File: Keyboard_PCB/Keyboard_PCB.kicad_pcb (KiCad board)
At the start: 6 copper layers, 65 x 103 mm, 119 parts, among them J2 Conn_ARM_SWD_TagConnect_TC2030, J3 CH_USB_C, SW1 BOOT, SW10 7, SW11 8, SW12 9, SW13 10, SW14 11, SW15 EC11E15244G1, SW2 NRST, SW3 0, SW4 1, SW5 2, SW6 3, SW7 4, SW8 5, SW9 6, U1 S40FC002C1B2I00000, U2 STM32U385VGI6, U3 CC2500, U4 2450BM15B0003001E, U5 USBLC6-2SC6, U6 ISL91127IRAZ, U7 MCP73833, Y1 26MHz, Y2 25MHz, Y3 32.786KHz

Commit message: Grid diode layout
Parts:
- added D10: D_Small, Marijn:SOD-523F, B.Cu at (208.0, 206.8)
- added D11: D_Small, Marijn:SOD-523F, B.Cu at (227.0, 206.8)
- added D12: D_Small, Marijn:SOD-523F, B.Cu at (188.9, 225.9)
- added D13: D_Small, Marijn:SOD-523F, B.Cu at (208.0, 225.9)
- added D14: D_Small, Marijn:SOD-523F, B.Cu at (227.0, 225.9)
- added D15: ~, Marijn:SOD-523F, F.Cu at (239.5, 154.6)
- added D3: D_Small, Marijn:SOD-523F, B.Cu at (196.5, 180.4)
- added D4: D_Small, Marijn:SOD-523F, B.Cu at (215.6, 180.4)
- added D5: D_Small, Marijn:SOD-523F, B.Cu at (234.6, 180.4)
- added D6: D_Small, Marijn:SOD-523F, B.Cu at (188.9, 187.8)
- added D7: D_Small, Marijn:SOD-523F, B.Cu at (208.0, 187.8)
- added D8: D_Small, Marijn:SOD-523F, B.Cu at (227.0, 187.8)
- added D9: D_Small, Marijn:SOD-523F, B.Cu at (188.9, 206.8)
- R21, R23: moved to F.Cu
- moved R20 20.3 mm to (237.9, 154.8), turned to 90 degrees
- moved C38 18.7 mm to (239.5, 151.7), turned to -90 degrees
- moved R21 18.4 mm to (219.3, 136.3), turned to 180 degrees
- moved R23 18.4 mm to (219.3, 137.8), turned to 180 degrees
- moved R22 16.6 mm to (237.9, 151.7), turned to -90 degrees
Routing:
- net /COL_1: track 0.00 -> 49.1 mm
- net /COL_0: track 0.00 -> 49.1 mm
- net /COL_2: track 0.00 -> 49.1 mm
- net /ROW_3: track 0.00 -> 38.1 mm
- net /ROW_2: track 0.00 -> 38.1 mm
- net /ROW_1: track 0.00 -> 38.1 mm
- net /ROW_0: track 0.00 -> 38.1 mm
- net /ROT_SW: track 0.00 -> 6.84 mm
- net Net-(D15-A): track 0.00 -> 5.57 mm
- net Net-(D9-A): track 0.00 -> 2.45 mm
- net Net-(D10-A): track 0.00 -> 2.45 mm
- net Net-(D11-A): track 0.00 -> 2.45 mm
- net Net-(D8-A): track 0.00 -> 2.45 mm
- net Net-(D7-A): track 0.00 -> 2.45 mm
- net Net-(D6-A): track 0.00 -> 2.45 mm
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
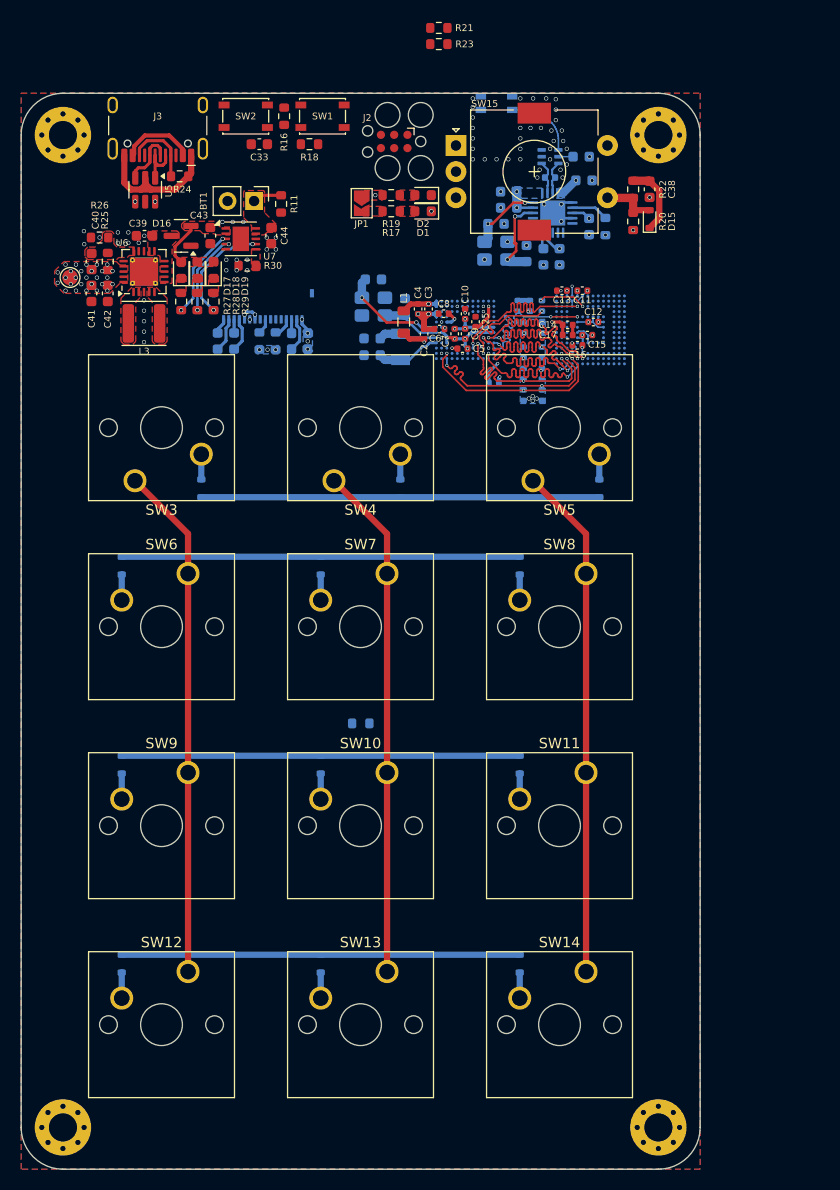
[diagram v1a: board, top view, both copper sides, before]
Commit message: Layout first draft
TODO: gnd stitching, check connections and schematic again
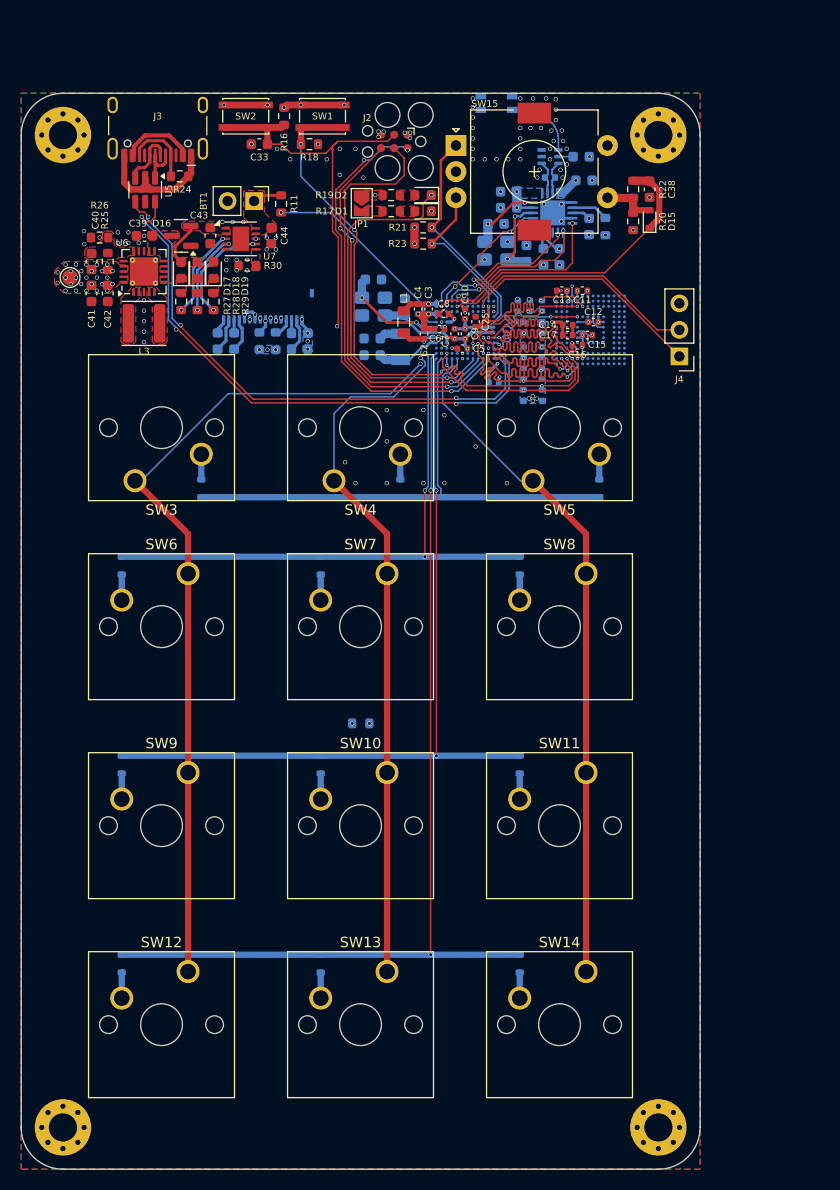
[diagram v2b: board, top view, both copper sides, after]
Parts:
- added J4: UART, Connector_PinHeader_2.54mm:PinHeader_1x03_P2.54mm_Vertical, F.Cu at (242.3, 167.7)
- moved R21 19.2 mm to (217.8, 155.4), turned to 0 degrees
- moved R23 19.2 mm to (217.8, 156.9), turned to 0 degrees
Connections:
- U2 pad L10: unconnected-(U2-PB10-PadL10) -> /UART_TX
- U2 pad L5: unconnected-(U2-PC5-PadL5) -> /UART_RX
- U2 pad M5: unconnected-(U2-PB0-PadM5) -> /OLED_RST
- U2 pad M6: unconnected-(U2-PB1-PadM6) -> /OLED_DC
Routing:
- net /ROW_3: track 38.1 -> 96.0 mm, vias 0 -> 2
- net /USB_DN: track 0.01 -> 55.1 mm, vias 1 -> 3
- net /USB_DP: track 0.01 -> 52.4 mm, vias 1 -> 3
- net /PWR/BAT_THERM: track 0.00 -> 51.8 mm, vias 0 -> 2
- net /NRST: track 0.00 -> 49.2 mm, vias 1 -> 2
- net /SWDIO: track 0.00 -> 42.3 mm, vias 0 -> 3
- net /SWCLK: track 0.00 -> 41.1 mm, vias 0 -> 1
- net /BOOT: track 0.00 -> 39.6 mm, vias 0 -> 3
- net /ROW_2: track 38.1 -> 76.3 mm, vias 0 -> 2
- net /STATUS: track 0.00 -> 36.9 mm, vias 0 -> 2
- net /COL_0: track 49.1 -> 85.3 mm, vias 0 -> 2
- net /SWO: track 0.00 -> 35.5 mm, vias 0 -> 3
- net /UART_RX: track 0.00 -> 24.6 mm, vias 0 -> 1
- net /OLED_SPI_NSS: track 0.00 -> 24.2 mm, vias 0 -> 2
- net /UART_TX: track 0.00 -> 23.2 mm, vias 0 -> 1
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
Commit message: Routing V1
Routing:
- net /PWR/VBUS: track 11.5 -> 27.2 mm, vias 0 -> 6
- net /BAT: track 2.81 -> 12.4 mm, vias 0 -> 3
- net GND: vias 128 -> 257
- net /STATUS: vias 2 -> 1

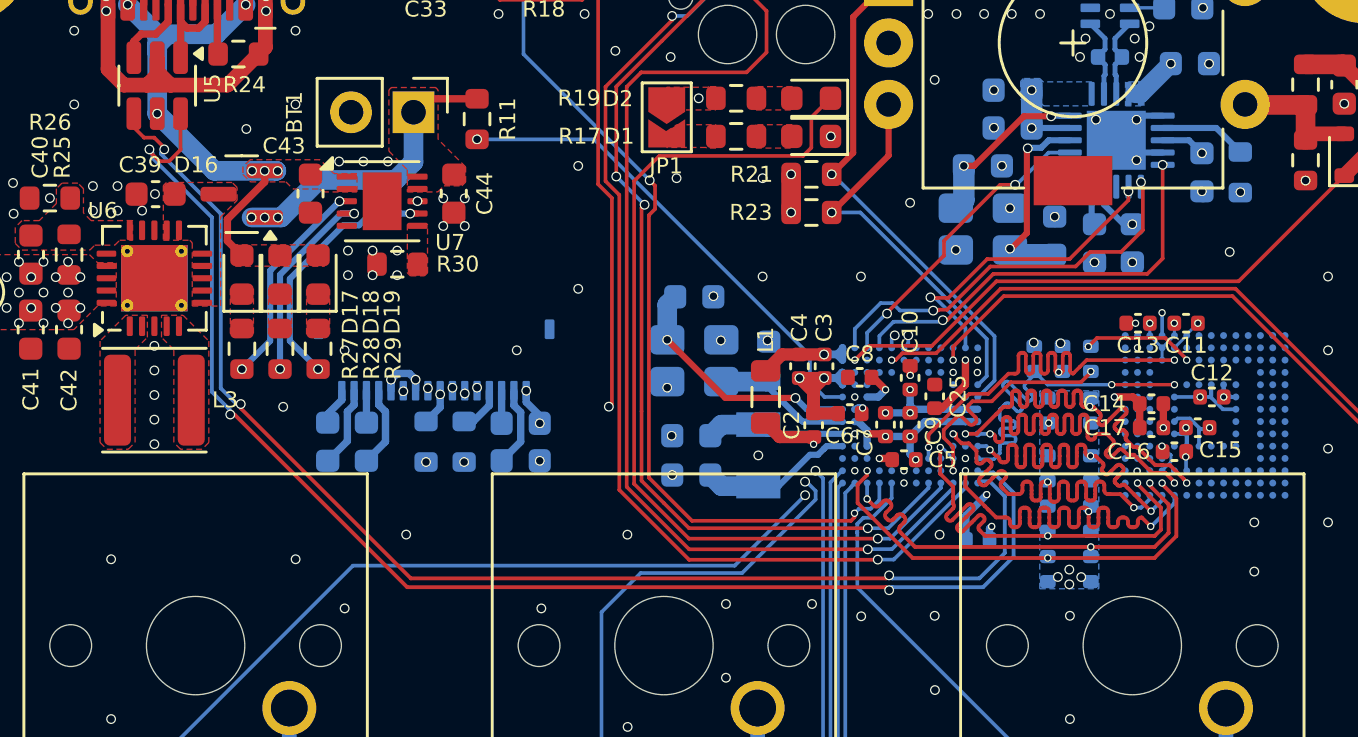
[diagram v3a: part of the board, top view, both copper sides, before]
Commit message: Added mouser IDs to components and checked STM-eMMC connection
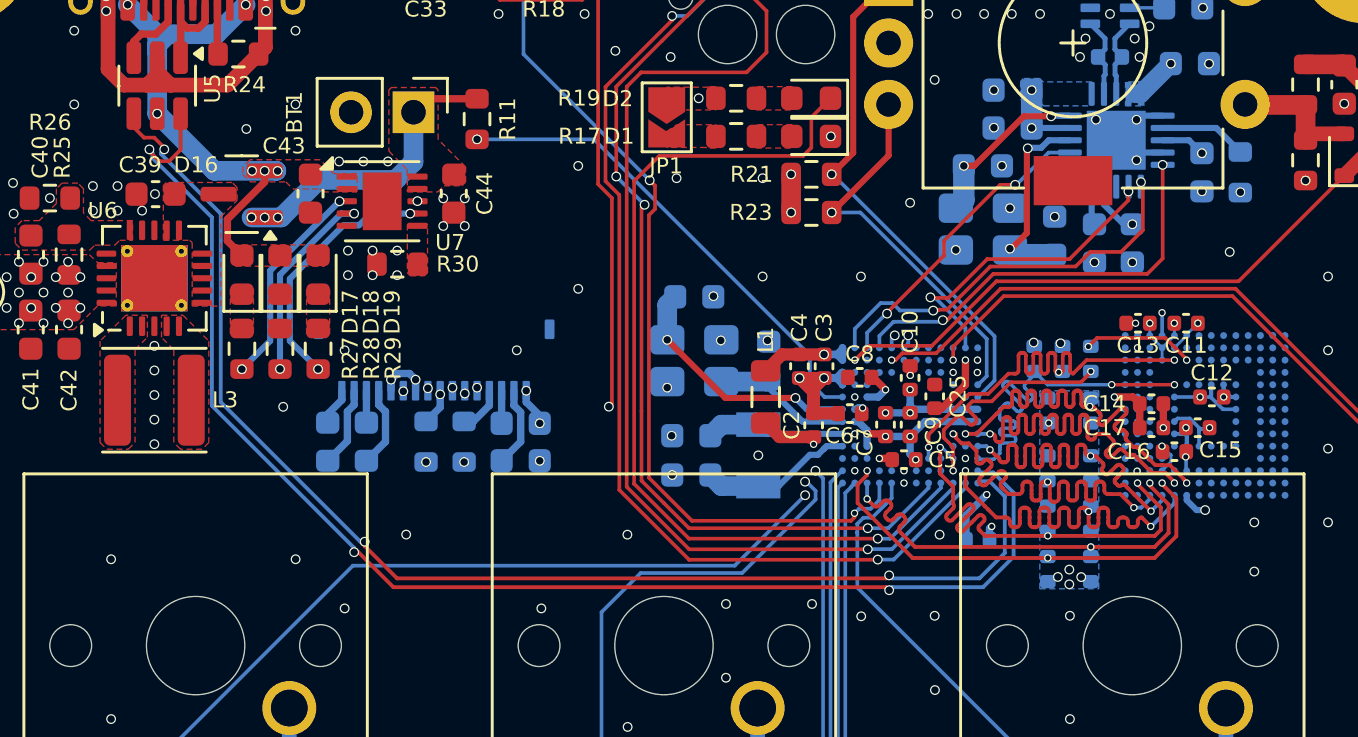
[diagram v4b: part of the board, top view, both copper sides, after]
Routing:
- net GND: track 56.3 -> 57.4 mm, vias 257 -> 258

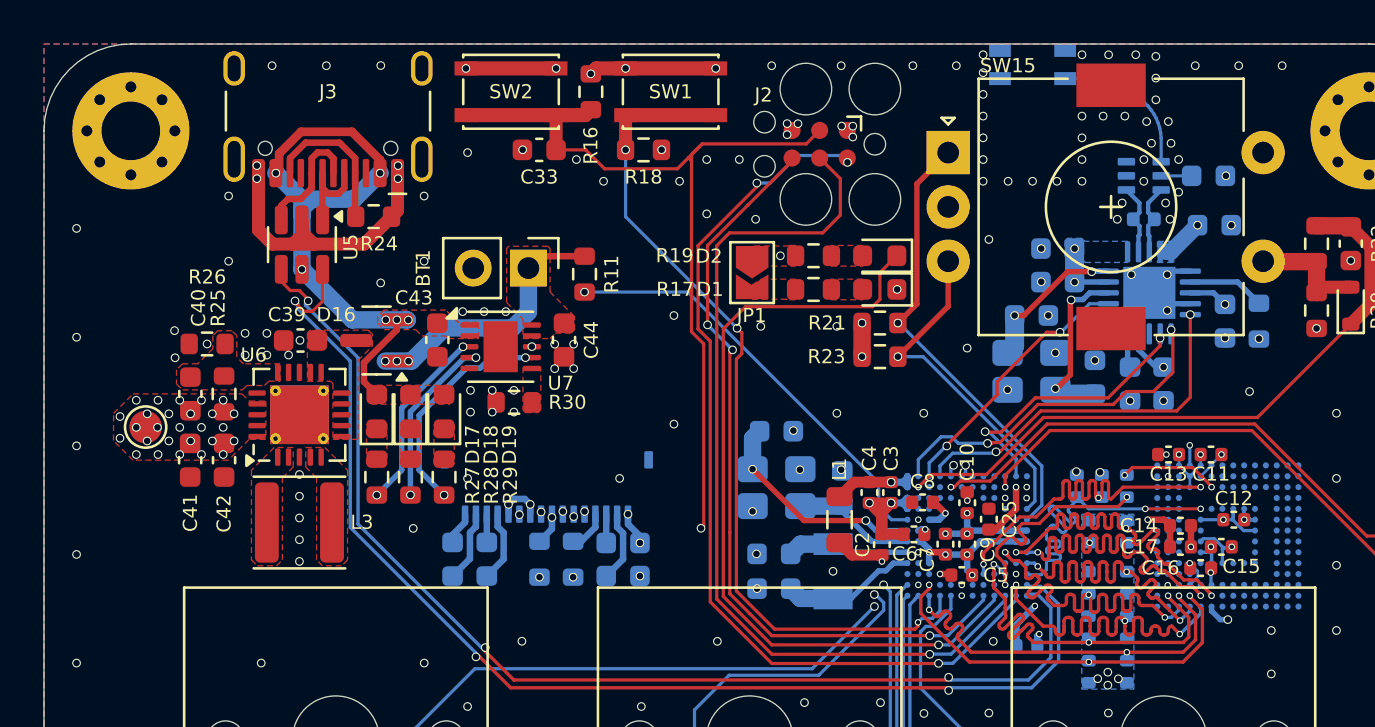
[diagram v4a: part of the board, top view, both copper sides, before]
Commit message: Added additional power filtering and improved RF path
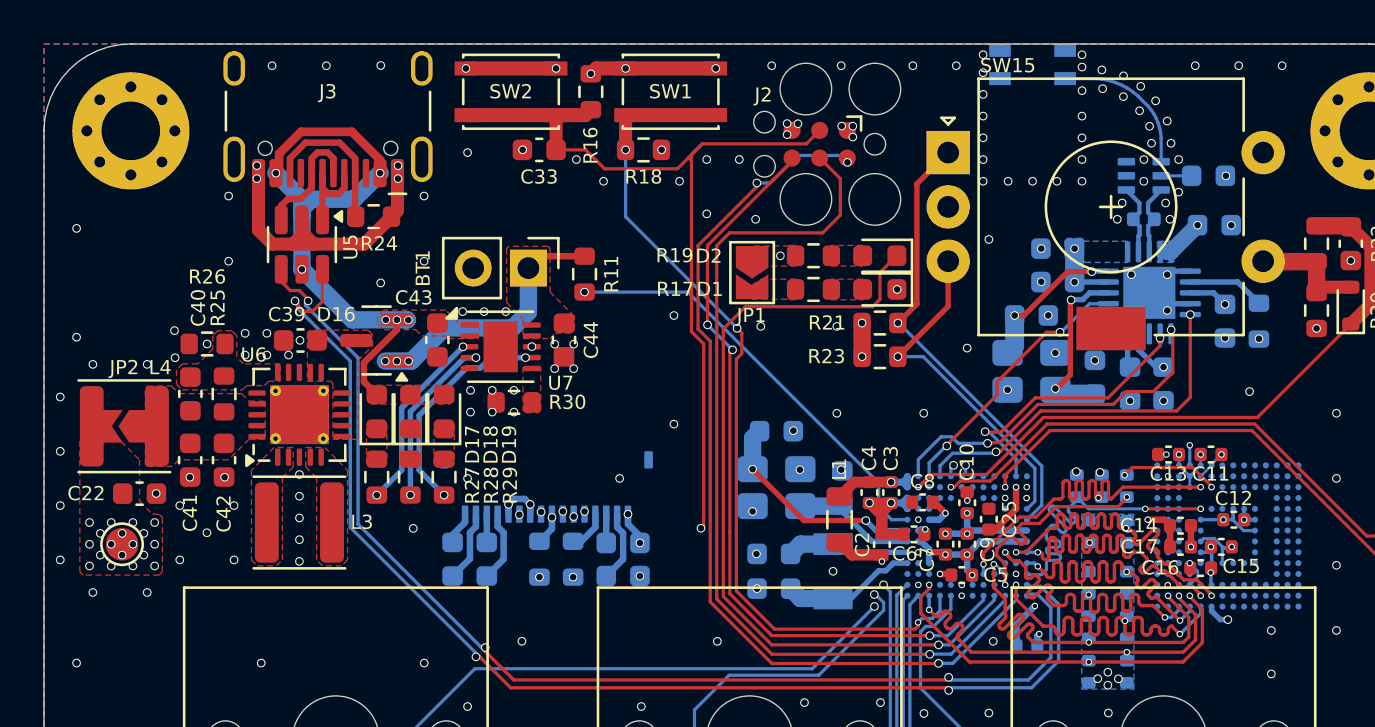
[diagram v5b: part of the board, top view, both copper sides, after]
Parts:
- added C22: 22u, Capacitor_SMD:C_0603_1608Metric, F.Cu at (183.7, 163.2)
- added JP2: LC_BYPASS, Jumper:SolderJumper-2_P1.3mm_Open_TrianglePad1.0x1.5mm, F.Cu at (183.0, 160.1)
- added L4: 1u, Inductor_SMD:L_APV_ANR4018, F.Cu at (183.0, 160.1)
- D10, D11, D12, D13, D14, D3, D4, D5, D6, D7, D8, D9: value D_Small -> ~
- D2: value CH_STATUS -> STATUS
- J3: value CH_USB_C -> USB_C
- moved TP1 5.50 mm to (182.9, 165.6)
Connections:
- C40 pad 1: +3V3 -> Net-(JP2-A)
- C41 pad 1: +3V3 -> Net-(JP2-A)
- C42 pad 1: +3V3 -> Net-(JP2-A)
- R25 pad 1: +3V3 -> Net-(JP2-A)
- U6 pad 17: +3V3 -> Net-(JP2-A)
- U6 pad 18: +3V3 -> Net-(JP2-A)
- U6 pad 19: +3V3 -> Net-(JP2-A)
- U6 pad 20: +3V3 -> Net-(JP2-A)
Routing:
- net GND: track 57.4 -> 57.5 mm, vias 258 -> 274
- net +3V3: vias 67 -> 58
- added copper zone on F.Cu, net Net-(JP2-A)
